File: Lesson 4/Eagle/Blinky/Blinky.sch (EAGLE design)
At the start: 10 parts, among them U1 NE555N

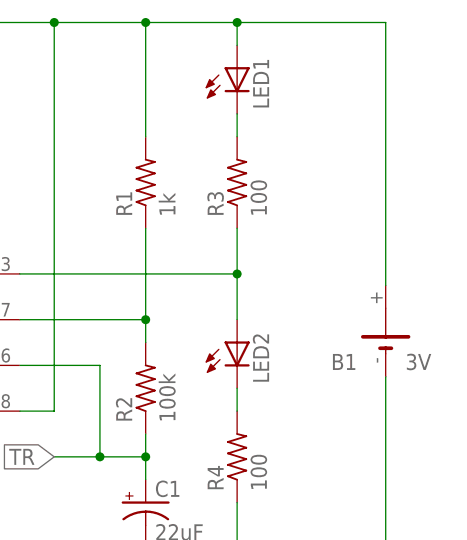
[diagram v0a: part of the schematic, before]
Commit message: Updates to the Lesson 4 Circuits
Updated schematics and board layout for Blinky and DIYPiano.
Created schematics for Light Siren.
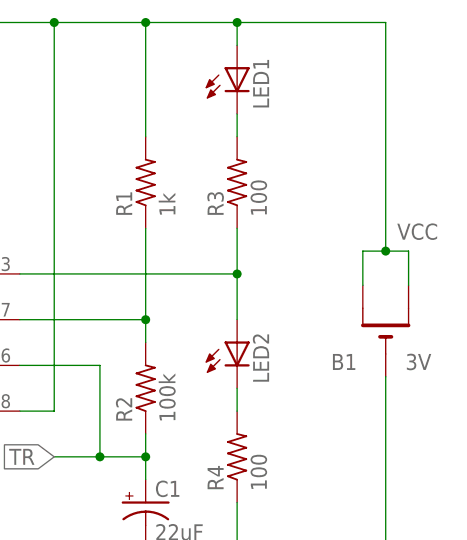
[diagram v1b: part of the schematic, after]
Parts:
- B1: device battery:CR2032H -> adafruit:CR1220THM
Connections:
- removed net N$3: B1.+, LED1.A, R1.2, U1.R, U1.V+
- new net VCC: B1.+, B1.+1, LED1.A, R1.2, U1.R, U1.V+
